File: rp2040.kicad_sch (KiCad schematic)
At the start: 24 parts, among them J2 Conn_01x03_Pin, U3 RP2040, U4 W25Q32JVSS, Y1 12MHz

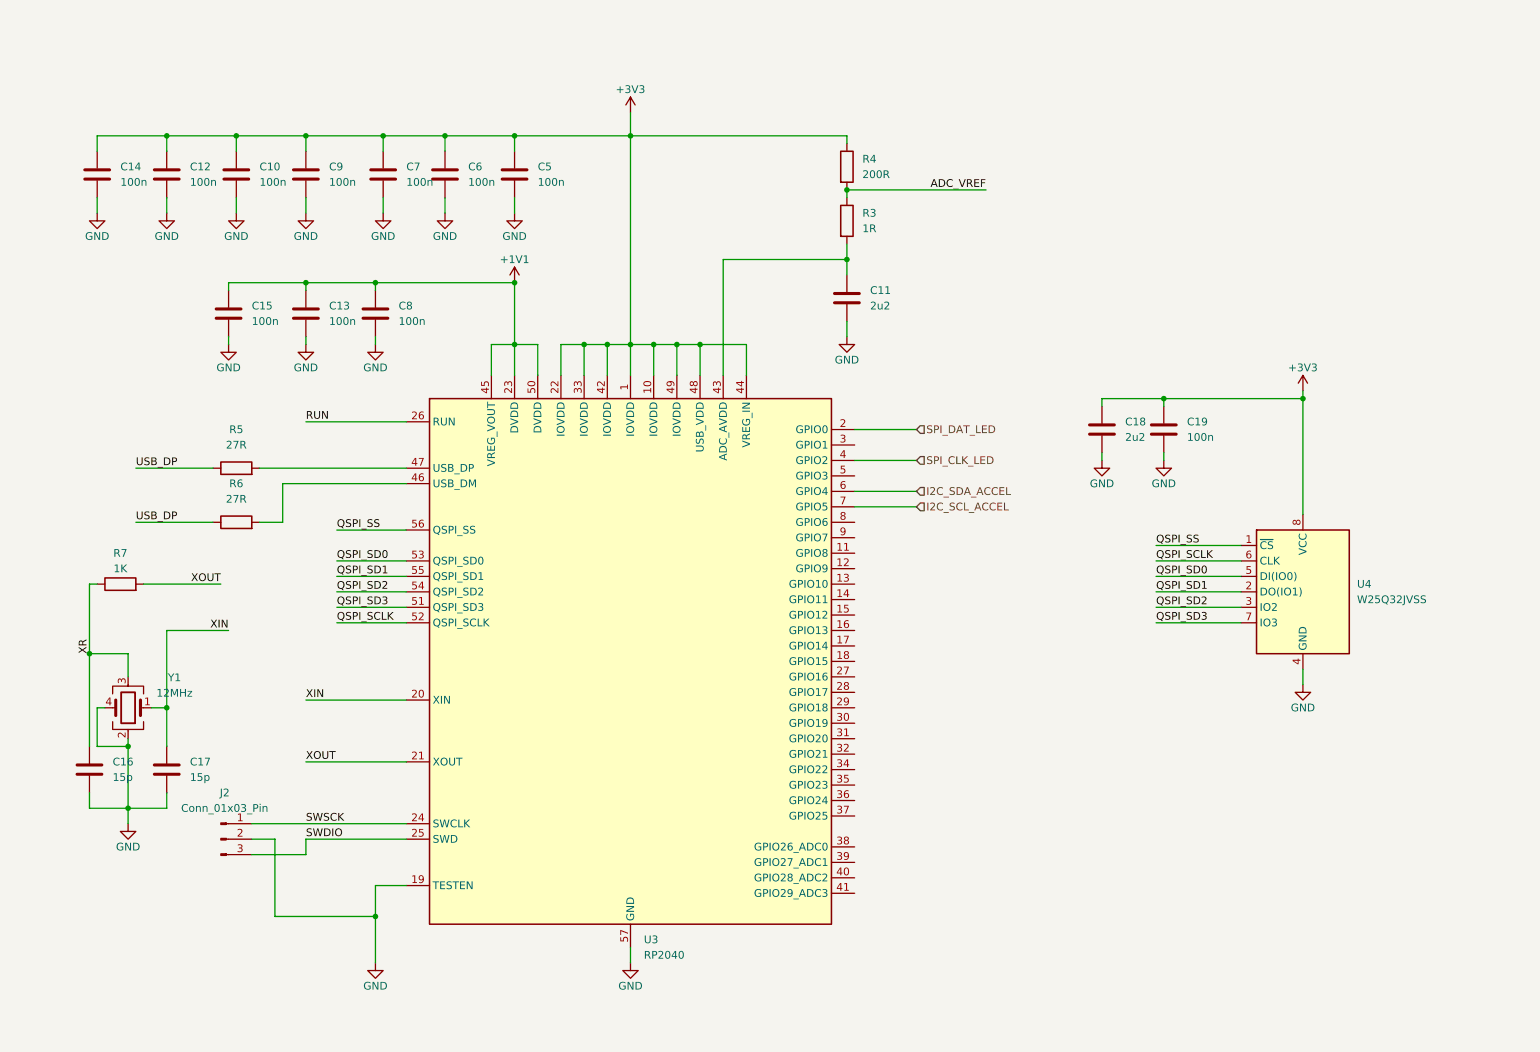
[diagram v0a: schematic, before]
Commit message: Added part numbers, footprints and improved formatting
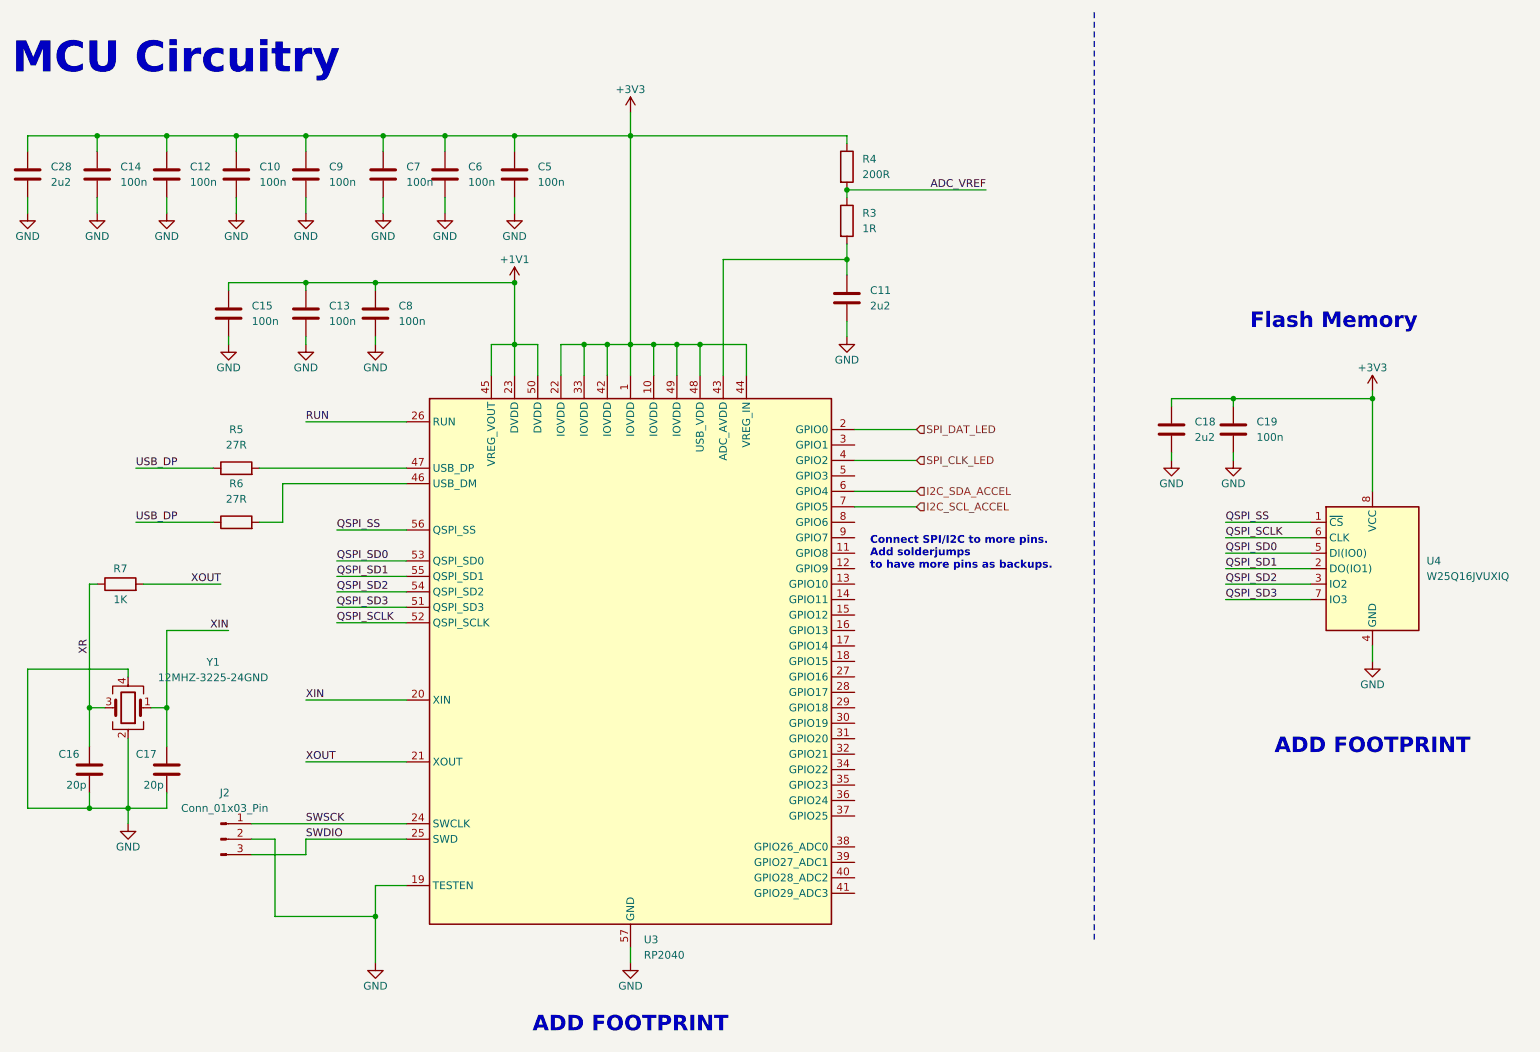
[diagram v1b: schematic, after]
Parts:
- added C28: 2u2, Capacitor_SMD:C_0805_2012Metric, symbol jellybeans:C-0805-2u2-25V
- C10, C12, C13, C14, C15, C5, C6, C7, C8, C9: footprint 0603 -> Capacitor_SMD:C_0603_1608Metric; symbol Device:C -> jellybeans:C-0603-100n-50V; JLC (none) -> C14663; MFG (none) -> YAGEO; MPN (none) -> CC0603KRX7R9BB104
- C11, C18: footprint (none) -> Capacitor_SMD:C_0805_2012Metric; symbol Device:C -> jellybeans:C-0805-2u2-25V; JLC (none) -> C377773; MFG (none) -> Samsung Electro-Mechanics; MPN (none) -> CL21A225KBQNNNE
- C16, C17: value 15p -> 20p; footprint (none) -> Capacitor_SMD:C_0402_1005Metric; symbol Device:C -> jellybeans:C-0402-20p-50V; JLC (none) -> C327010; MFG (none) -> YAGEO; MPN (none) -> CC0402FRNPO9BN200
- C19: footprint (none) -> Capacitor_SMD:C_0603_1608Metric; symbol Device:C -> jellybeans:C-0603-100n-50V; JLC (none) -> C14663; MFG (none) -> YAGEO; MPN (none) -> CC0603KRX7R9BB104
- R5, R6: footprint (none) -> Resistor_SMD:R_0603_1608Metric; symbol Device:R -> jellybeans:R-0402-27R; JLC (none) -> C25190; MFG (none) -> UNI-ROYAL(Uniroyal Elec); MPN (none) -> 0603WAF270JT5E
- R7: footprint (none) -> Resistor_SMD:R_0603_1608Metric; symbol Device:R -> jellybeans:R-0603-1K; JLC (none) -> C21190; MFG (none) -> UNI-ROYAL(Uniroyal Elec); MPN (none) -> 0603WAF1001T5E
- U3: footprint (none) -> LQFN-56 7x7; JLC (none) -> C2040; MFG (none) -> Raspberry Pi; MPN (none) -> RP2040
- U4: value W25Q32JVSS -> W25Q16JVUXIQ; symbol Memory_Flash:W25Q32JVSS -> suchi_chips:W25Q16JVUXIQ; JLC (none) -> C2843335; MFG (none) -> Winbond Elec; MPN (none) -> W25Q16JVUXIQ
- Y1: value 12MHz -> 12MHZ-3225-24GND; footprint (none) -> Crystal:Crystal_SMD_3225-4Pin_3.2x2.5mm; symbol Device:Crystal_GND23 -> suchi_crystals:12MHZ-3225-24GND; JLC (none) -> C9002; MFG (none) -> YXC Crystal Oscillators; MPN (none) -> X322512MSB4SI
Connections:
- net +3V3: now also C28.1
- net GND: now also C28.2
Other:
- note added: "ADD FOOTPRINT"
- note added: "Connect SPI/I2C to more pins. Add solderjumps to have more pins as backups."
- note added: "Flash Memory"
- note added: "MCU Circuitry"
- moved on the sheet: C18, C19, U4
